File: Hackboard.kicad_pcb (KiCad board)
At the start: 4 copper layers, 100 x 53.3 mm, 71 parts, among them J1 Conn_01x23_Socket, J2 Micro_SD_Card, J3 Conn_01x31_Socket, J4 Conn_01x08_Socket, J5 Conn_01x02_Pin, J6 USB_C_Receptacle_USB2.0_16P, J7 Barrel_Jack_Switch, Q1 NMOS, Q2 NMOS, Q3 NMOS, SW1 SW_SPST, U1 NCP164CSN330T1G, U2 AP63205WU, U3 STM32L476RGT6, U4 74LVC4245APW, U5 74LVC4245APW, U6 74LVC4245APW, U7 USBLC6-2SC6, U8 74LVC4245APW, U9 74LVC4245APW

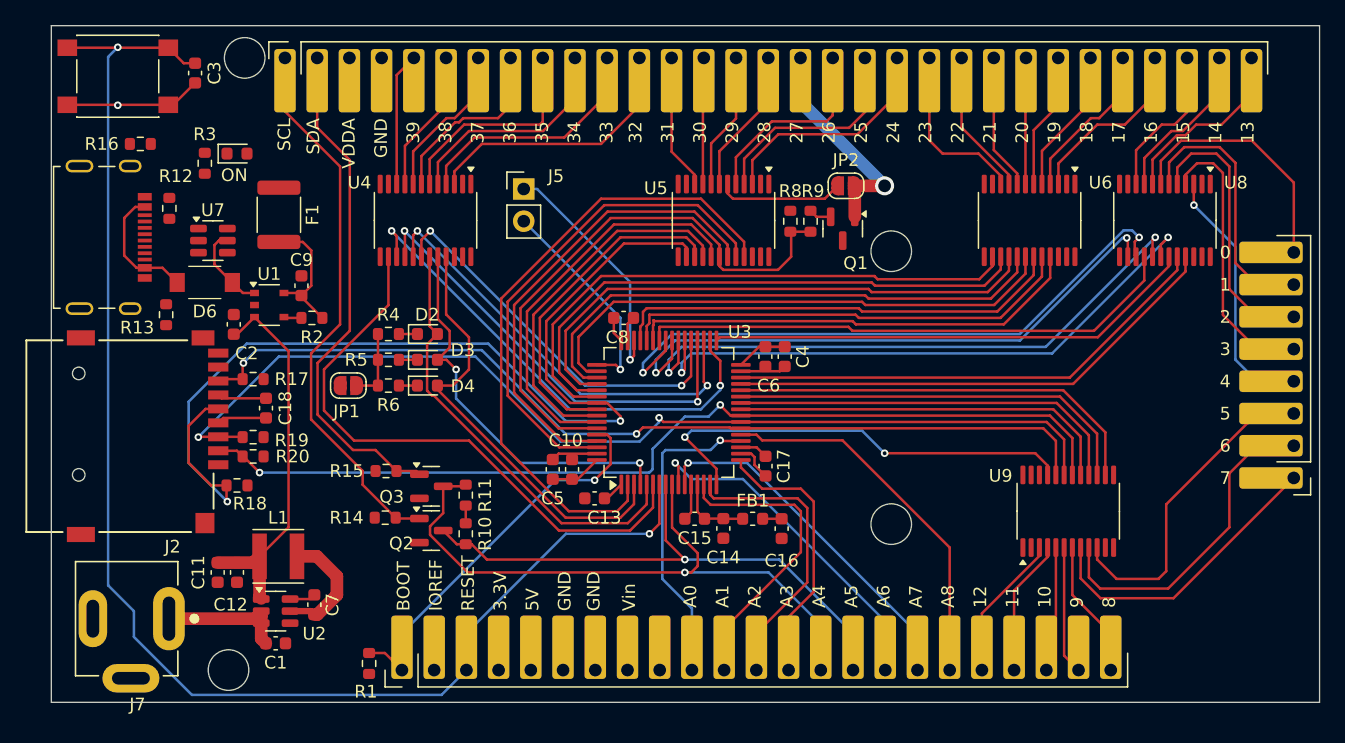
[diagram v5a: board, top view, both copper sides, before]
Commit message: Finish tracing power, add STEP files
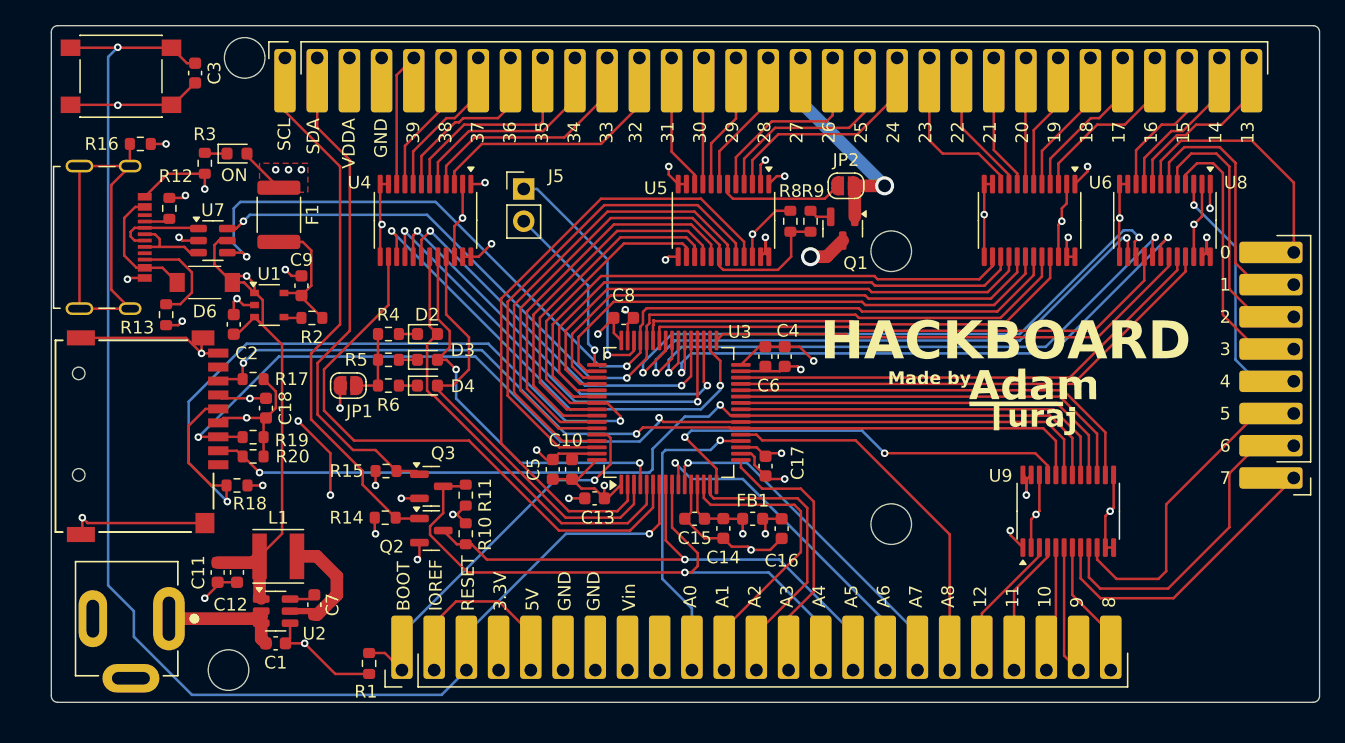
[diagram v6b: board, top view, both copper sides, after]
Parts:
- added G***: LOGO, Symbol:logo, F.Cu at (179.1, 105.2)
- moved SW1 0.25 mm to (107.2, 79.5)
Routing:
- net +5V: track 36.8 -> 250.5 mm, vias 0 -> 8
- net GND: track 29.9 -> 159.5 mm, vias 1 -> 31
- net VCC: track 9.77 -> 115.4 mm, vias 0 -> 1
- net VDDA: track 7.36 -> 99.3 mm, vias 0 -> 6
- net USB_DP_18: track 36.0 -> 80.9 mm, vias 0 -> 2
- net +3V3: track 19.6 -> 60.6 mm, vias 0 -> 17
- net USB_DM_17: track 36.1 -> 77.0 mm, vias 0 -> 2
- net Net-(J6-SHIELD): track 0.00 -> 33.5 mm
- net Net-(J6-CC2): track 0.00 -> 8.13 mm
- net Net-(J6-D--PadA7): track 0.00 -> 7.11 mm
- net Net-(J6-D+-PadA6): track 0.00 -> 6.38 mm
- net SW_SWCLK: track 16.8 -> 13.7 mm
- net Net-(J6-CC1): track 0.00 -> 2.02 mm
- net Net-(D1-K): track 0.00 -> 1.78 mm
- net DAC_A8: track 29.8 -> 30.4 mm
- added copper zone on F.Cu, net +3V3
- added copper zone on In2.Cu, net +3V3
- added copper zone on In1.Cu, net GND
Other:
- outline, holes or cut-outs redrawn
- board text added: "HACKBOARD"
- board text added: "Made by"

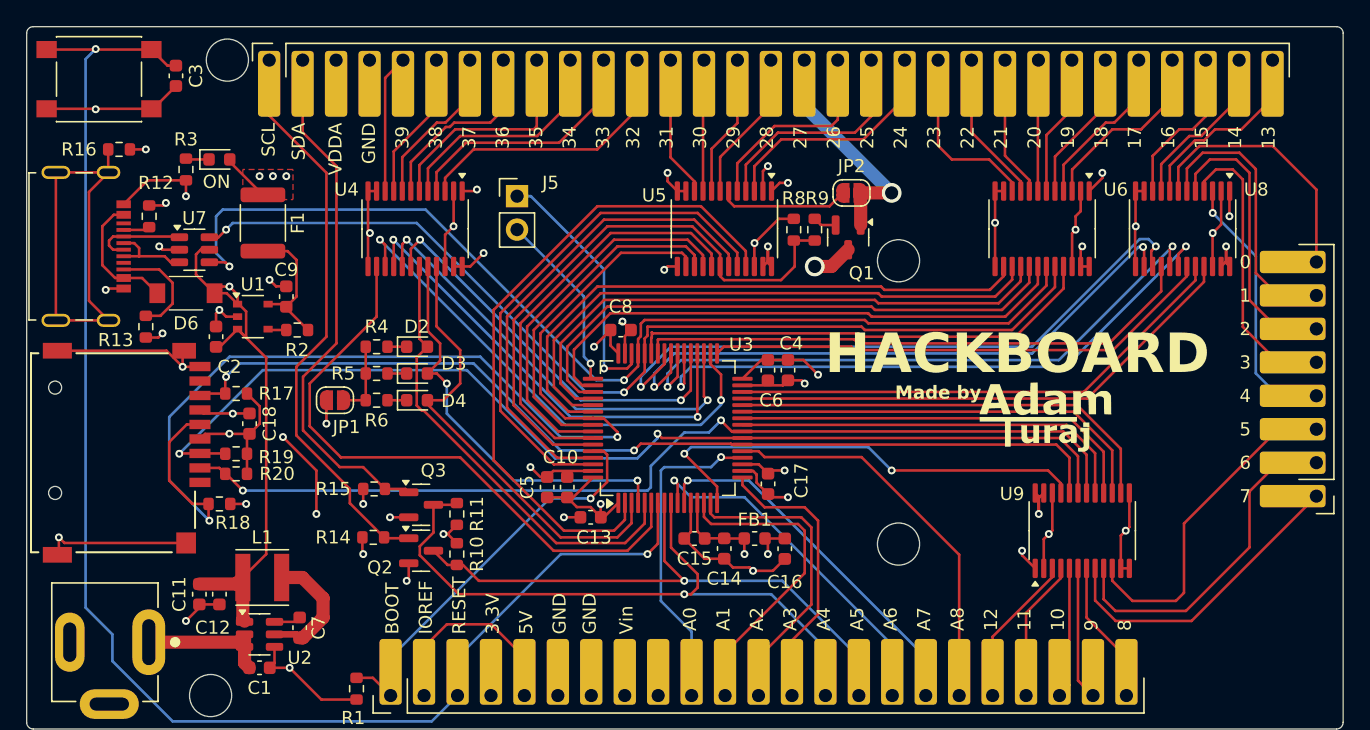
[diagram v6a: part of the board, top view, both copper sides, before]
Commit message: Change connector size, change USB port, add 3d models, add final touches
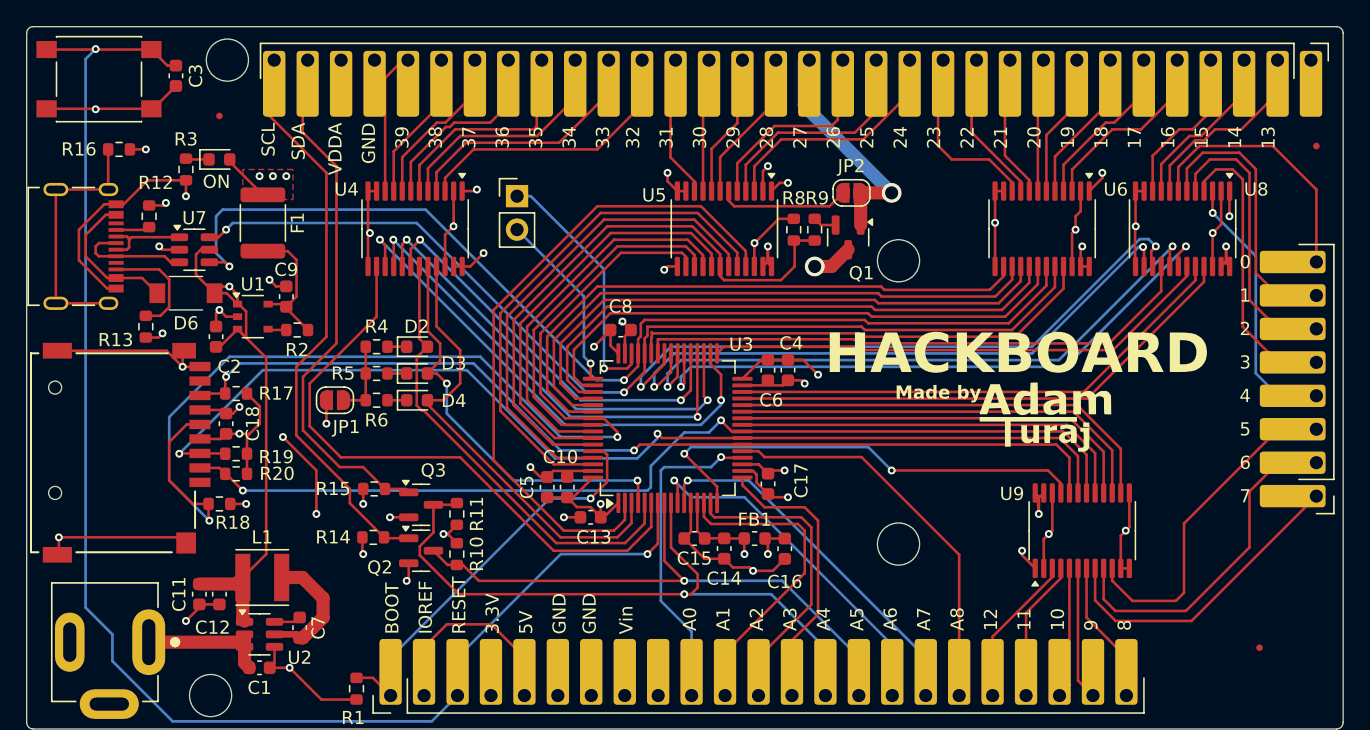
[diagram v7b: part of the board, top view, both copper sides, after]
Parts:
- added REF**: Fiducial_0.5mm_Mask1.5mm, Fiducial:Fiducial_0.5mm_Mask1.5mm, F.Cu at (195.3, 122.7)
- added REF**: Fiducial_0.5mm_Mask1.5mm, Fiducial:Fiducial_0.5mm_Mask1.5mm, F.Cu at (199.6, 84.6)
- added REF**: Fiducial_0.5mm_Mask1.5mm, Fiducial:Fiducial_0.5mm_Mask1.5mm, F.Cu at (116.3, 82.3)
- C7: value 100nF -> 0.1uF
- J3: value Conn_01x31_Socket -> Conn_01x32_Socket; footprint Connector_PinHeader_2.54mm:PinHeader_1x31_P2.54mm_Vertical -> Connector_PinHeader_2.54mm:PinHeader_1x32_P2.54mm_Vertical
- J6: footprint Connector_USB:USB_C_Receptacle_Molex_216990 -> Connector_USB:USB_C_Receptacle_Amphenol_GSB1C4
- moved J3 2.92 mm to (199.2, 78.1)
- moved C18 1.78 mm to (116.8, 105.7)
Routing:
- net Net-(J6-SHIELD): track 33.5 -> 19.7 mm
- net GND: track 159.5 -> 168.1 mm, vias 31 -> 30
- net Net-(J6-D+-PadA6): track 6.38 -> 8.81 mm
- net Net-(D6-A): track 10.00 -> 11.2 mm
- net Net-(J6-CC1): track 2.02 -> 2.60 mm

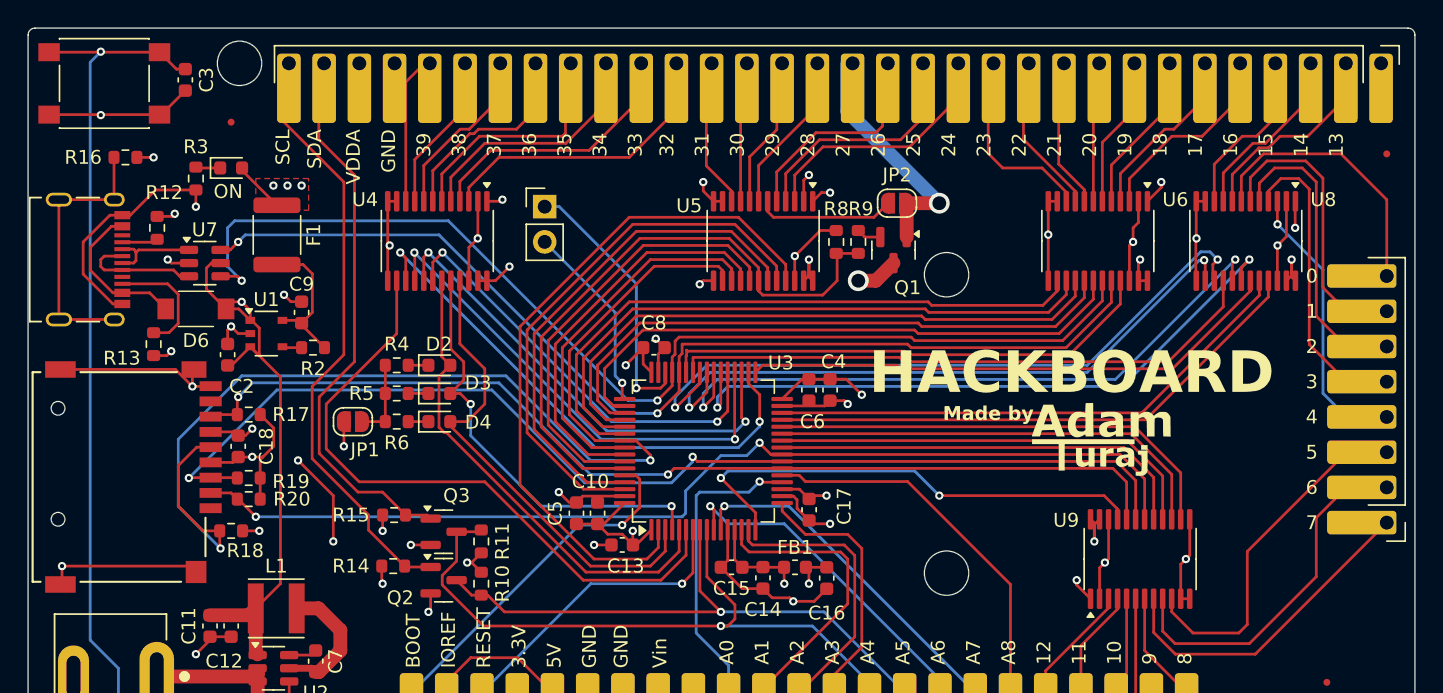
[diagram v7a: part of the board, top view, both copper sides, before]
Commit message: Change out LDO, add JLC parts
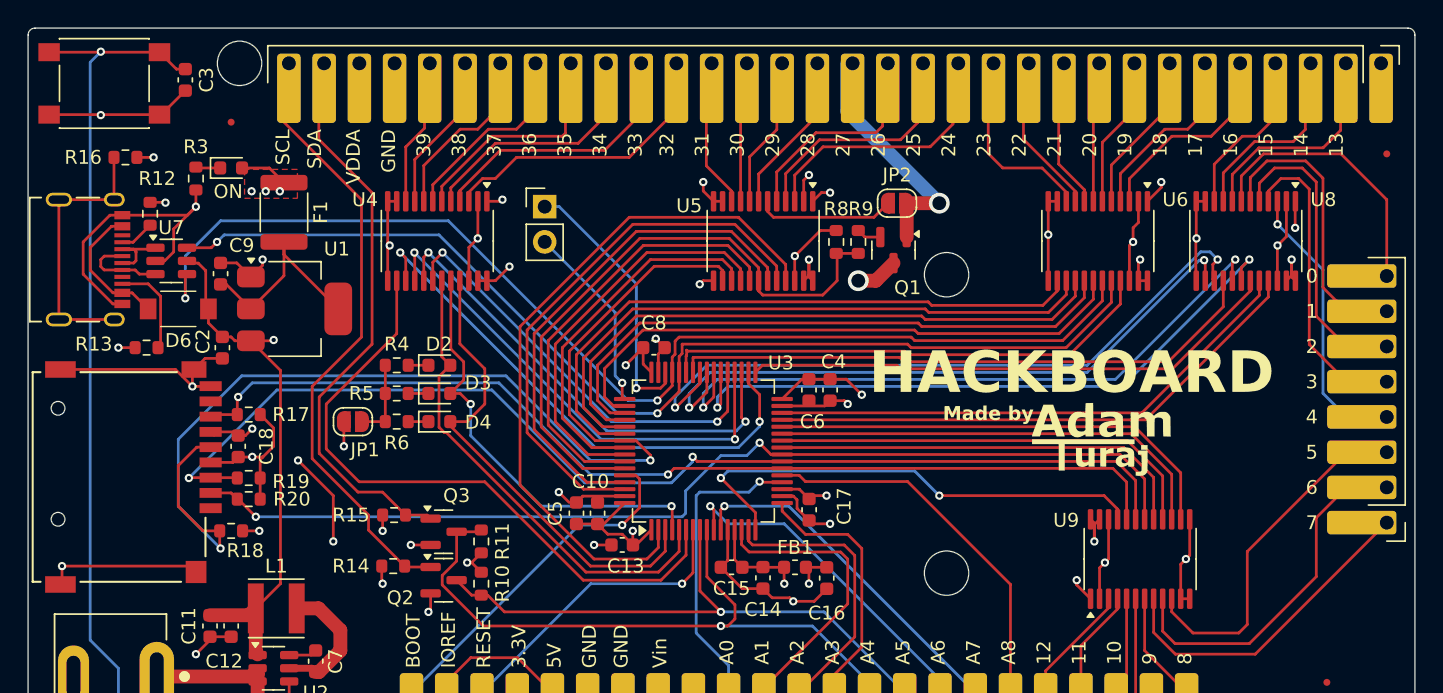
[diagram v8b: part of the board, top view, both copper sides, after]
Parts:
- removed R2: 10k, Resistor_SMD:R_0603_1608Metric
- C9: value 1uF -> 22uF
- L1: value 2uH -> 2.2uH
- R9: value 200R -> 220R
- U1: value NCP164CSN330T1G -> AMS1117-3.3; footprint Package_SO:TSOP-5_1.65x3.05mm_P0.95mm -> Package_TO_SOT_SMD:SOT-223-3_TabPin2
- U2: value AP63205WU -> AP63205WU-7
- moved C9 6.48 mm to (115.6, 93.2)
- moved U1 2.70 mm to (120.9, 95.8)
- moved U7 2.42 mm to (112.0, 92.3)
- moved F1 1.71 mm to (120.1, 88.8)
- moved D6 1.27 mm to (112.5, 95.8)
- moved R12 1.14 mm to (110.5, 88.9)
- moved C2 0.63 mm to (115.7, 98.6), turned to -90 degrees
- moved R13 0.57 mm to (110.2, 98.6), turned to 180 degrees
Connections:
- C9 pad 2: Net-(U1-OUT) -> Net-(U1-VO)
- F1 pad 2: Net-(U1-OUT) -> Net-(U1-VO)
- U1 pad 1: +5V -> GND
- U1 pad 2: GND -> Net-(U1-VO)
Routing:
- net Net-(U1-VO): track 0.00 -> 15.2 mm
- net Net-(U1-OUT): track 10.6 -> 0.00 mm
- net GND: track 168.1 -> 173.7 mm, vias 30 -> 28
- net USB_DP_18: track 80.9 -> 83.9 mm
- net Net-(J6-D+-PadA6): track 8.81 -> 6.17 mm
- net +5V: track 250.5 -> 247.9 mm
- net USB_DM_17: track 77.0 -> 79.4 mm
- net Net-(J6-CC2): track 8.49 -> 6.91 mm
- net Net-(J6-D--PadA7): track 6.76 -> 5.22 mm
- net +3V3: track 60.6 -> 59.2 mm
- net Net-(U1-PG): track 1.41 -> 0.00 mm
- net Net-(D6-A): track 11.2 -> 9.91 mm
- net PWM_13_O: track 14.8 -> 15.9 mm
- net PWM_14_O: track 12.9 -> 14.0 mm
- net SCL: track 43.7 -> 44.7 mm
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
